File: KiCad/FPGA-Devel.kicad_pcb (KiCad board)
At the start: 4 copper layers, 100 x 80 mm, 236 parts, among them J401 Conn_02x06_Top_Bottom, J402 Conn_02x06_Top_Bottom, J403 Conn_02x06_Top_Bottom, J404 USB_C_Receptacle_USB2.0_16P, J405 Conn_01x02_Pin, J801 USB_C_Receptacle_USB2.0_16P, Q201 BC847W, Q401 BC857W, Q402 BC857W, Q403 BC857W, Q404 BC857W, Q405 BC857W, SW401 SW_DIP_x04, SW402 SW_DIP_x04, SW403 SW_Omron_B3FS, SW404 SW_Omron_B3FS, SW405 SW_Omron_B3FS, SW406 SW_Omron_B3FS, SW407 SW_Omron_B3FS, SW408 SW_Omron_B3FS, SW409 SW_Omron_B3FS, SW410 SW_Omron_B3FS, SW411 SW_Omron_B3FS, SW412 RotaryEncoder_Switch, SW413 RKJXV1224, SW501 SW_Omron_B3FS, U1001 IS25LP032D-JNLE, U1002 APS6404, U201 TLV62568DDC, U202 TLV62568DDC, U203 TLV62568DDC, U401 LTC-4627JR, U502 XC7S50FTGB196, U801 FT2232HQ, U802 93LCxxB, U901 AP331, U902 74LVC2G53, X401 100MHz, Y801 12MHz

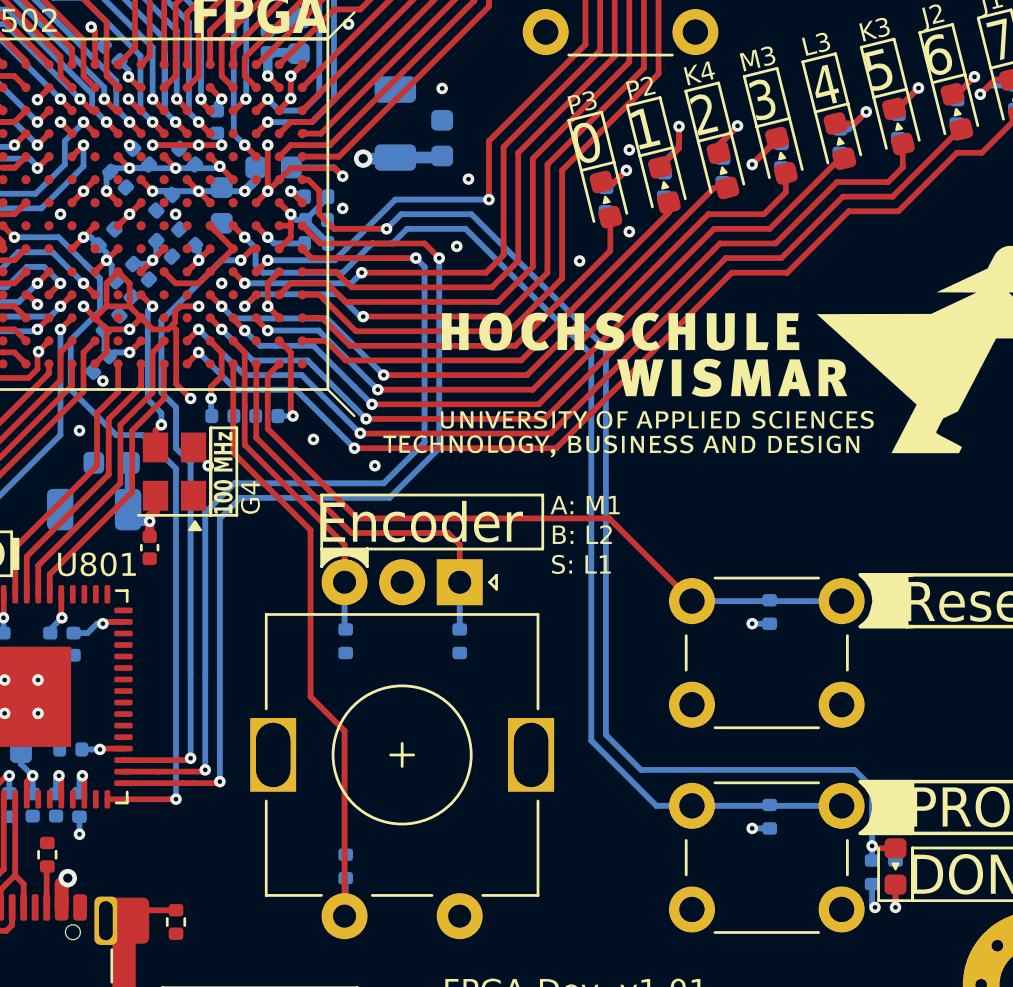
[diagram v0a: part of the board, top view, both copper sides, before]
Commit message: mehr kleine Layout-Anpassungen
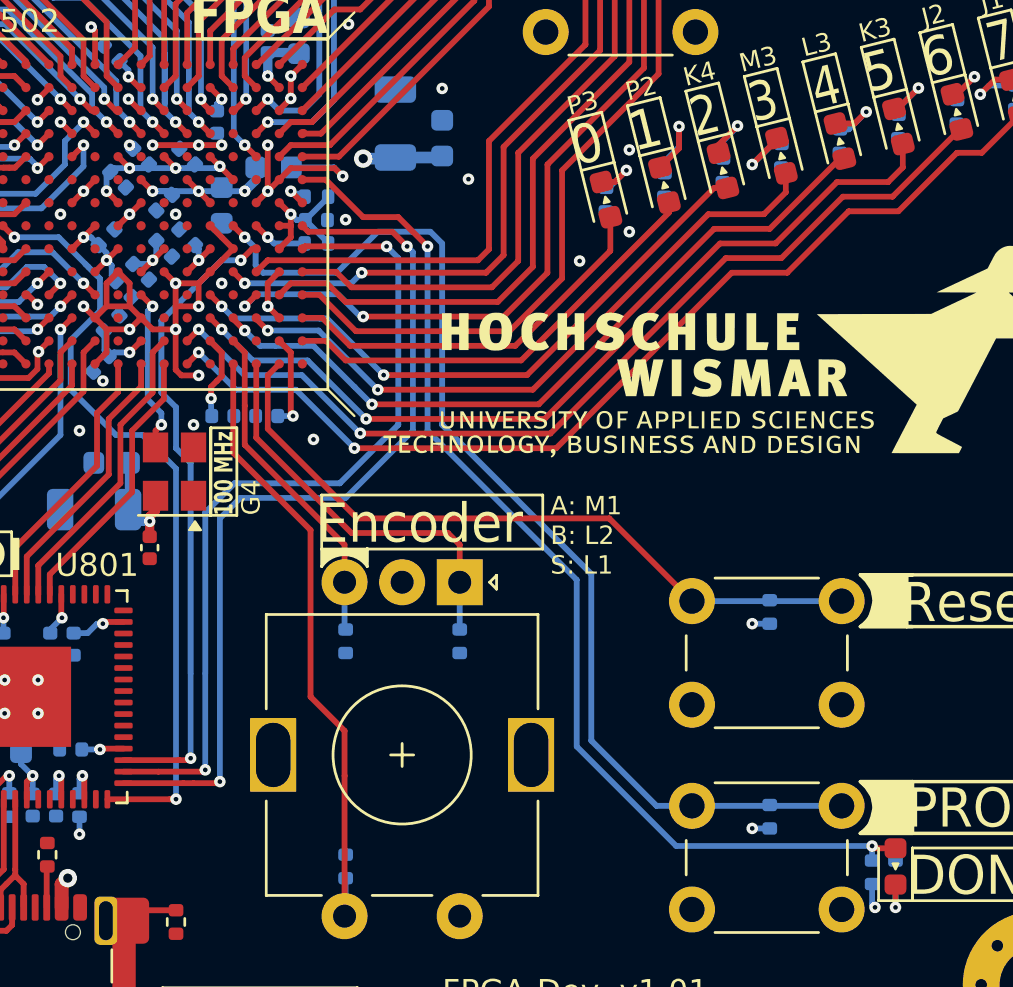
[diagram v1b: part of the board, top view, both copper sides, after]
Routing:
- net Net-(D501-A): track 50.8 -> 47.3 mm
- net /FT2232/JTAG.TDI: track 41.2 -> 38.6 mm
- net /FT2232/JTAG.TDO: track 38.8 -> 36.4 mm
- net GND: track 68.3 -> 70.0 mm
- net /IO/Btn.ZL: track 133.9 -> 135.1 mm, vias 2 -> 0
- net Net-(U502C-PROGRAM_B_0): track 48.7 -> 47.6 mm

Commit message: kleine Anpassungen im Silkscreen
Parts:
- added R449: 2k2, Resistor_SMD:R_0402_1005Metric, B.Cu at (80.0, 82.0)
- added R450: 2k2, Resistor_SMD:R_0402_1005Metric, B.Cu at (83.4, 82.0)
- added R451: 2k2, Resistor_SMD:R_0402_1005Metric, B.Cu at (92.7, 82.0)
- added R452: 2k2, Resistor_SMD:R_0402_1005Metric, B.Cu at (97.8, 82.0)
- added R453: 2k2, Resistor_SMD:R_0402_1005Metric, B.Cu at (87.6, 82.0)
- moved C401 9.09 mm to (90.2, 82.9), turned to 90 degrees
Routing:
- net Net-(Q405-B): track 6.81 -> 8.40 mm
- net Net-(Q402-B): track 6.21 -> 7.79 mm
- net Net-(Q401-B): track 5.84 -> 7.42 mm
- net Net-(Q404-B): track 6.80 -> 8.38 mm
- net Net-(Q403-B): track 6.81 -> 8.40 mm
- net /Connectors/PMOD.C4: track 32.7 -> 33.2 mm
- net +3.3V: track 91.2 -> 91.5 mm, vias 35 -> 36
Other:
- board text added: "'0' '1'"
- board text added: "'1' '0'"
- board text added: "FPGA-Dev. ${VERSION} Andreas Wenzel, ${CURRENT_DATE}"
- board text removed: "FPGA-Dev. v1.01 Andreas Wenzel, 22.10.2025"
